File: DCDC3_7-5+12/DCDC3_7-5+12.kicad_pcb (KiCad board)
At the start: 2 copper layers, 63.5 x 75.8 mm, 17 parts, among them T1 + 3.7V -, T2 + 12V -, T3 + 5V -, U1 XL6009, U2 XL6009

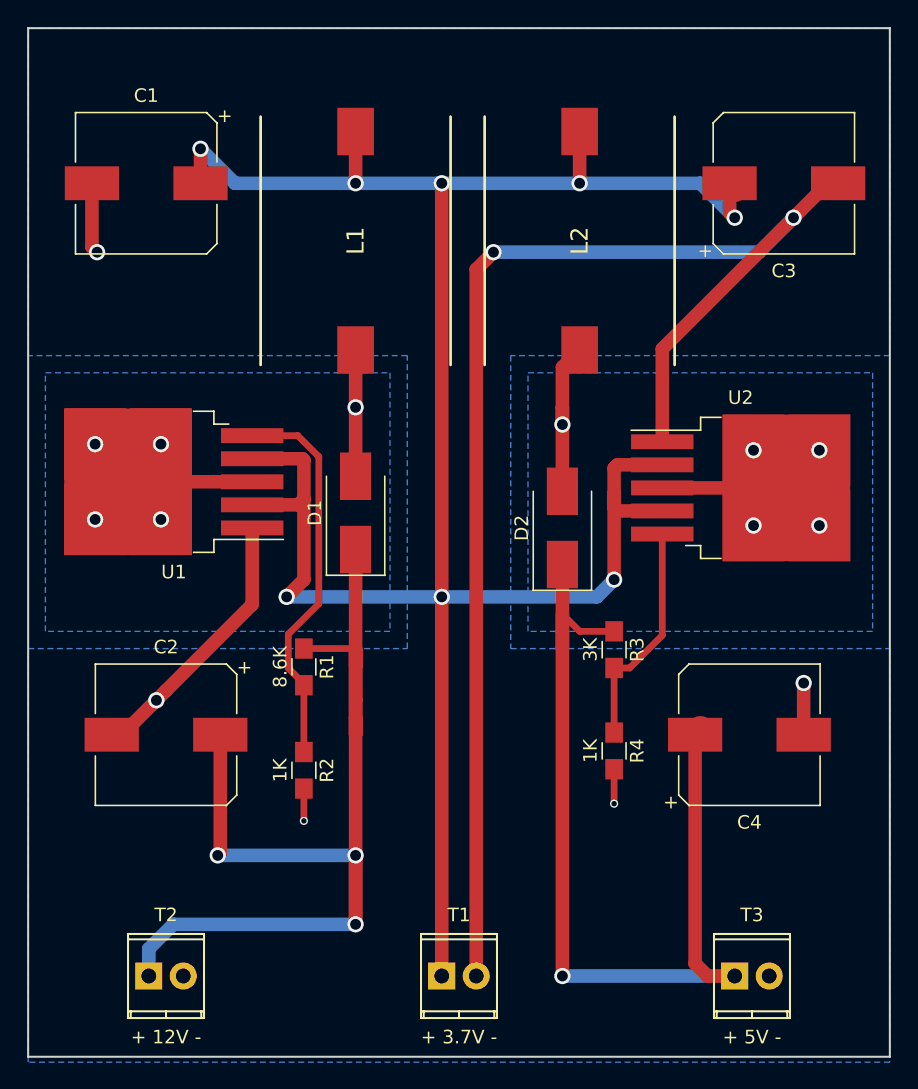
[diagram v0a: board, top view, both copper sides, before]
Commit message: Add mounting holes, adjust things to accomadate mounting holes.
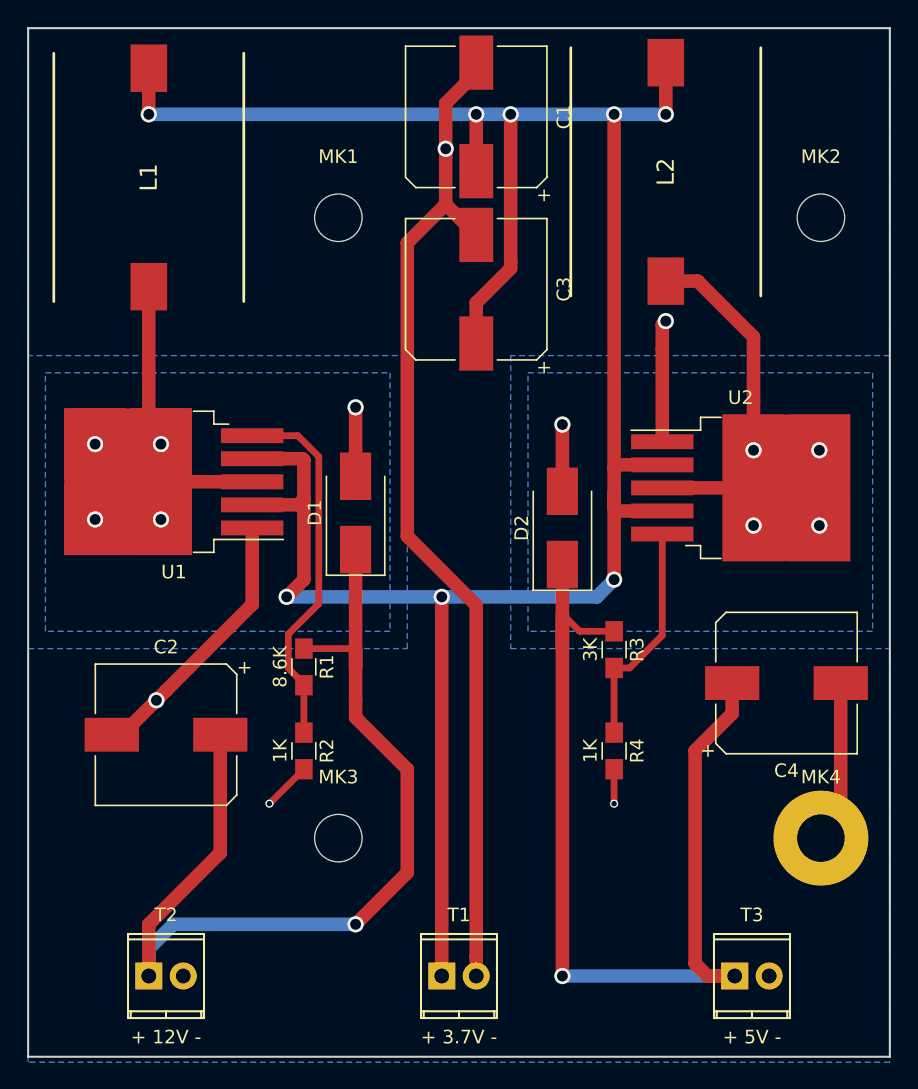
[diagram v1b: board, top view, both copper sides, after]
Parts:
- added MK1: Mounting_Hole, Mounting_Holes:MountingHole_3.5mm, F.Cu at (124.5, 77.5)
- added MK2: Mounting_Hole, Mounting_Holes:MountingHole_3.5mm, F.Cu at (160.0, 77.5)
- added MK3: Mounting_Hole, Mounting_Holes:MountingHole_3.5mm, F.Cu at (124.5, 123.2)
- added MK4: Mounting_Hole_PAD, Mounting_Holes:MountingHole_3.5mm_Pad, F.Cu at (160.0, 123.2)
- moved C1 24.8 mm to (134.6, 70.0), turned to 90 degrees
- moved C3 24.0 mm to (134.6, 82.7), turned to 90 degrees
- moved L1 15.9 mm to (110.5, 74.5)
- moved L2 8.13 mm to (148.6, 74.1)
- moved C4 4.69 mm to (157.5, 111.8)
- moved R2 1.43 mm to (121.9, 116.8)
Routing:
- net /DCDC 3.7 - 12/GND: track 136.3 -> 122.4 mm, vias 7 -> 5
- net Net-(D2-Pad2): track 25.1 -> 34.4 mm
- net /DCDC 3.7 - 12/12V: track 82.8 -> 74.3 mm, vias 3 -> 1
- net /DCDC 3.7 - 12/3.7V: track 173.0 -> 181.1 mm
- net Net-(D1-Pad2): track 18.5 -> 26.2 mm
- net /DCDC 3.7 to 5/5V: track 70.6 -> 75.0 mm
- net Net-(R1-Pad2): track 28.7 -> 27.3 mm

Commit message: Add FAN header, minor trace updates.
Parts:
- added J1: FAN, Pin_Headers:Pin_Header_Straight_1x02_Pitch2.54mm, F.Cu at (153.7, 128.3)
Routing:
- net /DCDC 3.7 - 12/GND: track 122.4 -> 64.0 mm
- net /DCDC 3.7 - 12/3.7V: track 181.1 -> 213.4 mm, vias 8 -> 6
- net /DCDC 3.7 to 5/5V: track 75.0 -> 80.1 mm
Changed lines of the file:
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@@
 (kicad_pcb (version 4) (host pcbnew 4.0.7+dfsg1-1ubuntu2)
   (general
-    (links 43)
+    (links 45)
     (no_connects 0)
-    (area 101.524999 63.424999 165.175001 139.375001)
+    (area 101.524999 54.45 183.11 139.700001)
     (thickness 1.6)
     (drawings 12)
     (tracks 131)
     (zones 0)
-    (modules 21)
+    (modules 22)
     (nets 9)
   )
@@
       (net 2 "/DCDC 3.7 - 12/GND"))
   )
+  (module Pin_Headers:Pin_Header_Straight_1x02_Pitch2.54mm (layer F.Cu)
+    (at 153.67 128.27 90)
+    (descr "Through hole straight pin header, 1x02, 2.54mm pitch, single row")
+    (tags "Through hole pin header THT 1x02 2.54mm single row")
+    (fp_text reference J1 (at 0 -2.33 90) (layer F.SilkS)
+      (effects (font (size 1 1) (thickness 0.15)))
+    )
+    (fp_text value FAN (at 0 4.87 90) (layer F.SilkS)
+      (effects (font (size 1 1) (thickness 0.15)))
+    )
+    (fp_line (start -0.635 -1.27) (end 1.27 -1.27) (layer F.Fab) (width 0.1))
+    (fp_line (start 1.27 -1.27) (end 1.27 3.81) (layer F.Fab) (width 0.1))
+    (fp_line (start 1.27 3.81) (end -1.27 3.81) (layer F.Fab) (width 0.1))
+    (fp_line (start -1.27 3.81) (end -1.27 -0.635) (layer F.Fab) (width 0.1))
+    (fp_line (start -1.27 -0.635) (end -0.635 -1.27) (layer F.Fab) (width 0.1))
+    (fp_line (start -1.33 3.87) (end 1.33 3.87) (layer F.SilkS) (width 0.12))
+    (fp_line (start -1.33 1.27) (end -1.33 3.87) (layer F.SilkS) (width 0.12))
+    (fp_line (start 1.33 1.27) (end 1.33 3.87) (layer F.SilkS) (width 0.12))
+    (fp_line (start -1.33 1.27) (end 1.33 1.27) (layer F.SilkS) (width 0.12))
+    (fp_line (start -1.33 0) (end -1.33 -1.33) (layer F.SilkS) (width 0.12))
+    (fp_line (start -1.33 -1.33) (end 0 -1.33) (layer F.SilkS) (width 0.12))
+    (fp_line (start -1.8 -1.8) (end -1.8 4.35) (layer F.CrtYd) (width 0.05))
+    (fp_line (start -1.8 4.35) (end 1.8 4.35) (layer F.CrtYd) (width 0.05))
+    (fp_line (start 1.8 4.35) (end 1.8 -1.8) (layer F.CrtYd) (width 0.05))
+    (fp_line (start 1.8 -1.8) (end -1.8 -1.8) (layer F.CrtYd) (width 0.05))
+    (fp_text user %R (at 0 1.27 180) (layer F.Fab)
+      (effects (font (size 1 1) (thickness 0.15)))
+    )
+    (pad 1 thru_hole rect (at 0 0 90) (size 1.7 1.7) (drill 1) (layers *.Cu *.Mask)
+      (net 4 "/DCDC 3.7 to 5/5V"))
+    (pad 2 thru_hole oval (at 0 2.54 90) (size 1.7 1.7) (drill 1) (layers *.Cu *.Mask)
+      (net 2 "/DCDC 3.7 - 12/GND"))
+    (model ${KISYS3DMOD}/Pin_Headers.3dshapes/Pin_Header_Straight_1x02_Pitch2.54mm.wrl
+      (at (xyz 0 0 0))
+      (scale (xyz 1 1 1))
+      (rotate (xyz 0 0 0))
+    )
+  )
   (gr_line (start 160.02 77.47) (end 124.46 77.47) (layer Dwgs.User) (width 0.2))
   (gr_line (start 160.02 123.19) (end 160.02 77.47) (layer Dwgs.User) (width 0.2))
@@
   (gr_line (start 165.1 63.5) (end 165.1 139.3) (layer Edge.Cuts) (width 0.15))
   (gr_line (start 101.6 63.5) (end 165.1 63.5) (layer Edge.Cuts) (width 0.15))
+  (segment (start 144.78 97.79) (end 144.78 100.33) (width 1) (layer F.Cu) (net 1))
+  (segment (start 144.78 100.33) (end 132.08 100.33) (width 1) (layer F.Cu) (net 1))
+  (segment (start 132.08 100.33) (end 132.08 105.41) (width 1) (layer F.Cu) (net 1))
+  (segment (start 132.08 105.41) (end 132.08 133.35) (width 1) (layer F.Cu) (net 1))
+  (segment (start 118.11 133.35) (end 132.08 133.35) (width 1) (layer B.Cu) (net 1))
+  (via (at 118.11 133.35) (size 1.2) (drill 0.8) (layers F.Cu B.Cu) (net 1))
+  (segment (start 120.65 105.41) (end 118.899999 107.160001) (width 1) (layer F.Cu) (net 1))
+  (segment (start 118.899999 107.160001) (end 118.899999 119.649999) (width 1) (layer F.Cu) (net 1))
+  (segment (start 118.899999 119.649999) (end 118.11 120.439998) (width 1) (layer F.Cu) (net 1))
+  (segment (start 118.11 120.439998) (end 118.11 133.35) (width 1) (layer F.Cu) (net 1))
   (segment (start 134.62 69.85) (end 110.49 69.85) (width 1) (layer B.Cu) (net 1))
   (segment (start 137.16 69.85) (end 134.62 69.85) (width 1) (layer B.Cu) (net 1))
@@
   (segment (start 144.78 95.93) (end 144.78 97.79) (width 1) (layer F.Cu) (net 1))
   (segment (start 144.78 97.79) (end 144.78 98.83) (width 1) (layer F.Cu) (net 1))
-  (segment (start 144.78 104.14) (end 144.78 97.79) (width 1) (layer F.Cu) (net 1))
-  (segment (start 132.08 105.41) (end 143.51 105.41) (width 1) (layer B.Cu) (net 1))
-  (segment (start 143.51 105.41) (end 144.78 104.14) (width 1) (layer B.Cu) (net 1))
-  (via (at 144.78 104.14) (size 1.2) (drill 0.8) (layers F.Cu B.Cu) (net 1))
-  (segment (start 132.08 133.35) (end 132.08 105.41) (width 1) (layer F.Cu) (net 1))
-  (segment (start 120.65 105.41) (end 132.08 105.41) (width 1) (layer B.Cu) (net 1))
-  (via (at 132.08 105.41) (size 1.2) (drill 0.8) (layers F.Cu B.Cu) (net 1))
   (segment (start 121.92 98.2) (end 121.92 104.14) (width 1) (layer F.Cu) (net 1))
   (segment (start 121.92 104.14) (end 120.65 105.41) (width 1) (layer F.Cu) (net 1))
-  (via (at 120.65 105.41) (size 1.2) (drill 0.8) (layers F.Cu B.Cu) (net 1))
   (segment (start 144.78 98.83) (end 145.03 99.08) (width 1) (layer F.Cu) (net 1))
   (segment (start 145.03 99.08) (end 148.33 99.08) (width 1) (layer F.Cu) (net 1))
@@
   (segment (start 121.92 98.2) (end 121.92 95.323516) (width 1) (layer F.Cu) (net 1))
   (segment (start 118.11 98.63) (end 121.49 98.63) (width 1) (layer F.Cu) (net 1))
+  (segment (start 132.37 76.49) (end 132.08 76.78) (width 1) (layer F.Cu) (net 2))
+  (segment (start 134.62 131.936508) (end 134.62 133.35) (width 1) (layer F.Cu) (net 2))
   (via (at 119.38 120.65) (size 0.6) (drill 0.4) (layers F.Cu B.Cu) (net 2))
   (segment (start 121.92 118.11) (end 119.38 120.65) (width 0.5) (layer F.Cu) (net 2))
-  (segment (start 129.54 79.32) (end 129.54 100.945998) (width 1) (layer F.Cu) (net 2))
-  (segment (start 129.54 100.945998) (end 134.62 106.025998) (width 1) (layer F.Cu) (net 2))
-  (segment (start 134.62 131.936508) (end 134.62 133.35) (width 1) (layer F.Cu) (net 2))
-  (segment (start 134.62 106.025998) (end 134.62 131.936508) (width 1) (layer F.Cu) (net 2))
   (segment (start 161.48 111.76) (end 161.48 121.73) (width 1) (layer F.Cu) (net 2))
   (segment (start 161.48 121.73) (end 160.02 123.19) (width 1) (layer F.Cu) (net 2))
-  (segment (start 132.37 76.49) (end 129.54 79.32) (width 1) (layer F.Cu) (net 2))
   (segment (start 148.33 87.14) (end 148.33 85.35) (width 1) (layer F.Cu) (net 2))
   (segment (start 148.33 85.35) (end 148.59 85.09) (width 1) (layer F.Cu) (net 2))
@@
   (segment (start 121.92 109.22) (end 125.73 109.22) (width 0.5) (layer F.Cu) (net 3))
   (segment (start 115.57 115.38) (end 115.76 115.57) (width 2) (layer F.Cu) (net 3))
+  (segment (start 153.67 133.35) (end 153.67 128.27) (width 1) (layer F.Cu) (net 4))
   (segment (start 153.48 111.76) (end 153.48 114.01) (width 1) (layer F.Cu) (net 4))
   (segment (start 153.48 114.01) (end 150.75 116.74) (width 1) (layer F.Cu) (net 4))

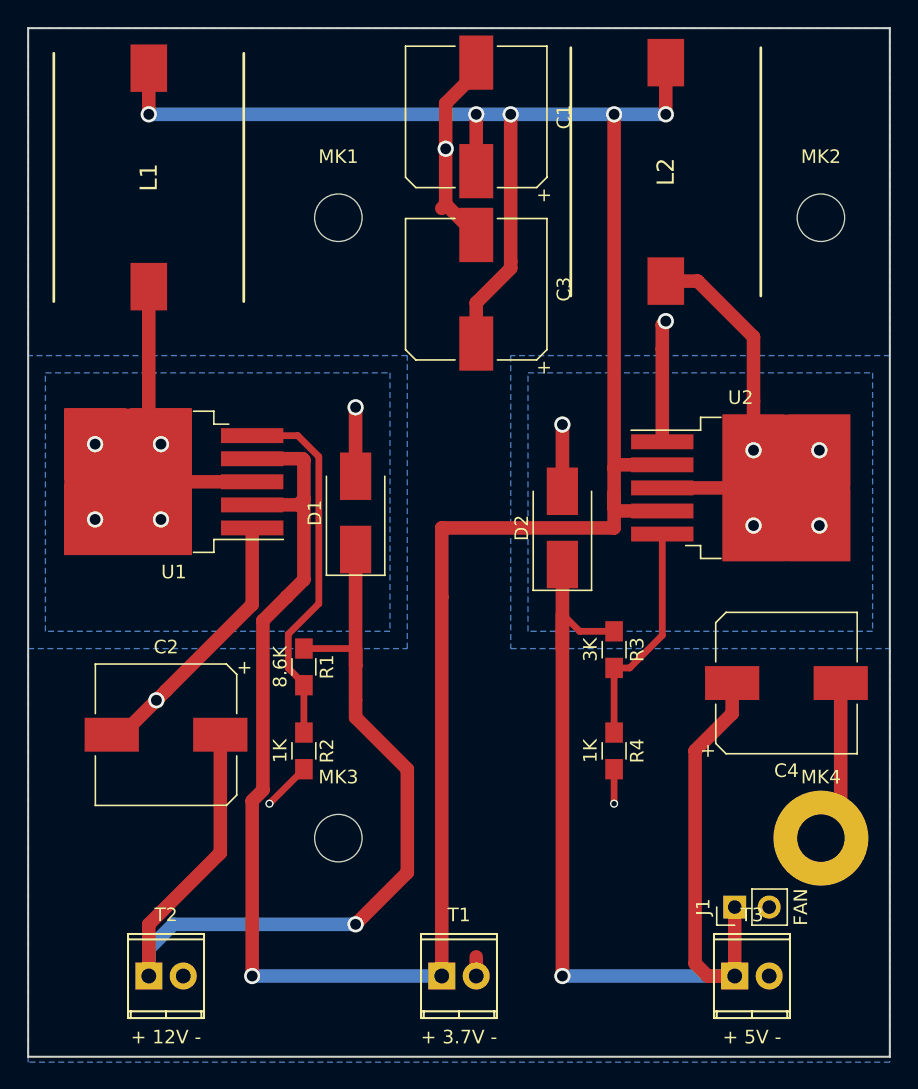
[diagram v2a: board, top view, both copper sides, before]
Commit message: Nearly complete circuit for the AUX power supply.
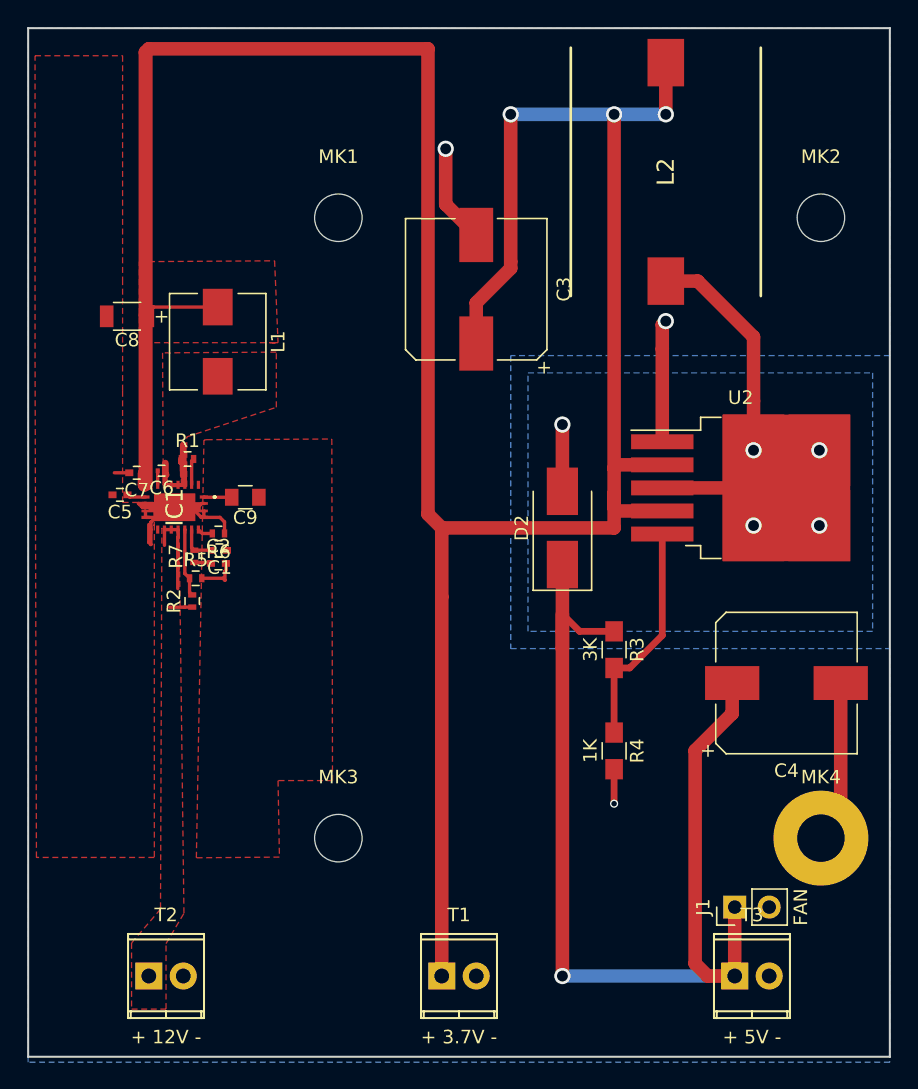
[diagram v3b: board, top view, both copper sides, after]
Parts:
- removed D1: SS34, Diodes_SMD:D_SMB_Handsoldering
- removed U1: XL6009, TO_SOT_Packages_SMD:TO-263-5_TabPin3
- added C5: 47nf, Capacitors_SMD:C_0402, F.Cu at (108.4, 97.9)
- added C6: .1uf, Capacitors_SMD:C_0201, F.Cu at (111.4, 96.1)
- added C7: .1uf, Capacitors_SMD:C_0402, F.Cu at (109.6, 96.3)
- added C8: 10uf, MyCaps:C_1206_Pol, F.Cu at (108.9, 84.7)
- added C9: 3.3uf, Capacitors_SMD:C_0805, F.Cu at (117.6, 98.1)
- added IC1: TPS61088QRHLRQ1, TPS61088QRHLRQ1:TPS61088QRHLRQ1, F.Cu at (112.4, 98.8)
- added R5: 56K, Resistors_SMD:R_0402, F.Cu at (113.9, 104.0)
- added R6: 49.9K, Resistors_SMD:R_0402, F.Cu at (115.6, 100.7)
- added R7: R, Resistors_SMD:R_0402, F.Cu at (113.8, 102.4)
- C1, C2: value 220uf 50V -> C_Small; footprint Capacitors_SMD:CP_Elec_10x10.5 -> Capacitors_SMD:C_0402
- L1: value 33uH -> 1.5uh; footprint PM5022S-330M-RC:INDPM183140X690N -> Inductors_SMD:L_Wuerth_HCI-7040
- R1: value 8.6K -> 290K; footprint Resistors_SMD:R_0805_HandSoldering -> Resistors_SMD:R_0402
- R2: value 1K -> 500K; footprint Resistors_SMD:R_0805_HandSoldering -> Resistors_SMD:R_0402
- moved C1 37.1 mm to (115.7, 102.0), turned to 180 degrees
- moved R1 17.6 mm to (113.3, 95.2), turned to 0 degrees
- moved R2 13.8 mm to (113.7, 105.7), turned to 90 degrees
- moved C2 13.2 mm to (115.6, 102.9), turned to 0 degrees
- moved L1 13.1 mm to (115.6, 86.6)
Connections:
- C1 pad 1: /DCDC 3.7 - 12/3.7V -> GND
- C1 pad 2: /DCDC 3.7 - 12/GND -> Net-(C1-Pad2)
- C2 pad 1: /DCDC 3.7 - 12/12V -> Net-(C2-Pad1)
- C2 pad 2: /DCDC 3.7 - 12/GND -> GND
- C3 pad 2: /DCDC 3.7 - 12/GND -> GND
- C4 pad 2: /DCDC 3.7 - 12/GND -> GND
- J1 pad 2: /DCDC 3.7 - 12/GND -> GND
- L1 pad 2: Net-(D1-Pad2) -> Net-(C6-Pad1)
- MK4 pad 1: /DCDC 3.7 - 12/GND -> GND
- R1 pad 1: /DCDC 3.7 - 12/12V -> Net-(C6-Pad1)
- R1 pad 2: Net-(R1-Pad2) -> Net-(IC1-Pad3)
- R2 pad 1: Net-(R1-Pad2) -> /DCDC 3.7 - 12/12V
- R2 pad 2: /DCDC 3.7 - 12/GND -> Net-(IC1-Pad17)
- R4 pad 2: /DCDC 3.7 - 12/GND -> GND
- T1 pad 2: /DCDC 3.7 - 12/GND -> GND
- T2 pad 2: /DCDC 3.7 - 12/GND -> GND
- T3 pad 2: /DCDC 3.7 - 12/GND -> GND
- U2 pad 1: /DCDC 3.7 - 12/GND -> GND
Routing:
- net /DCDC 3.7 - 12/12V: track 74.3 -> 8.40 mm, vias 1 -> 0
- net /DCDC 3.7 - 12/GND: track 64.0 -> 0.00 mm, vias 5 -> 0
- net GND: track 0.00 -> 63.7 mm, vias 0 -> 3
- net /DCDC 3.7 - 12/3.7V: track 213.4 -> 244.9 mm, vias 6 -> 3
- net Net-(R1-Pad2): track 27.3 -> 0.00 mm
- net Net-(D1-Pad2): track 26.2 -> 0.00 mm, vias 5 -> 0
- net Net-(C6-Pad1): track 0.00 -> 14.2 mm
- net Net-(IC1-Pad17): track 0.00 -> 5.05 mm
- net Net-(C1-Pad2): track 0.00 -> 2.91 mm
- net Net-(C9-Pad2): track 0.00 -> 2.06 mm
- net Net-(IC1-Pad3): track 0.00 -> 1.96 mm
- net Net-(C5-Pad1): track 0.00 -> 1.40 mm
- net Net-(C2-Pad1): track 0.00 -> 1.26 mm
- net Net-(IC1-Pad19): track 0.00 -> 1.14 mm
- net Net-(C6-Pad2): track 0.00 -> 1.04 mm
- added copper zone on F.Cu, net /DCDC 3.7 - 12/12V
- added copper zone on F.Cu, net /DCDC 3.7 - 12/3.7V
- added copper zone on B.Cu, net GND
- added copper zone on F.Cu, net GND
- added copper zone on F.Cu, net Net-(C6-Pad1)
- removed copper zone on B.Cu, net /DCDC 3.7 - 12/GND
- removed copper zone on B.Cu, net Net-(D1-Pad2)
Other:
- net class Default: clearance 0.2 -> 0.1
- rule trace_clearance: 0.2 -> 0.1
